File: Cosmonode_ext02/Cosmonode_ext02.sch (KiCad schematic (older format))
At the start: 19 parts, among them J1 CONN_01X04, J2 CONN_01X04, J3 CONN_01X08, J4 CONN_01X08, J5 GS3, J6 GS3, Q1 BSS138, Q2 BSS138, SW1 SW_Push, SW2 SW_Push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

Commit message: big push!
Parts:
- added J7: Aloes_Logo, Aloes:Aloes_mini, symbol CONN_01X01
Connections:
- net +5V: now also J1.1 (P1), J2.1 (P1); no longer J1.4 (P4), J2.4 (P4)
- net D3_5V: now also J1.2 (P2); no longer J1.3 (P3)
- net D4_5V: now also J2.2 (P2); no longer J2.3 (P3)
- net A6: now reaches J3.8 (P8)
- net A7: now reaches J4.8 (P8)
- net at C1.2, SW1.1: now also J1.4 (P4); no longer J1.1 (P1)
- net at C1.1, C2.2, C3.2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: now also J1.3 (P3), J2.3 (P3); no longer J1.2 (P2), J2.2 (P2)
- net at C5.2, SW2.1: now also J2.4 (P4); no longer J2.1 (P1)
- no-connect marks 6 -> 9
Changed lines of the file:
@@
 LIBS:valves
 LIBS:BSS138
-LIBS:XC6206P302MR_SOT23_
-LIBS:Cosmonode_ext02_v0.3-cache
+LIBS:Cosmonode_ext02-cache
 EELAYER 25 0
 EELAYER END
@@
 F 3 "" H 4200 2700 50  0001 C CNN
 	1    4200 2700
-	-1   0    0    1
+	-1   0    0    -1
 $EndComp
 $Comp
@@
 F 3 "" H 7250 2700 50  0001 C CNN
 	1    7250 2700
-	-1   0    0    1
+	-1   0    0    -1
 $EndComp
 $Comp
@@
 Text Notes 4250 2450 2    60   ~ 0
 SENSOR
+Text Label 7250 5400 2    60   ~ 0
+A6
+Text Label 8200 5400 2    60   ~ 0
+A7
+NoConn ~ 8200 5400
+NoConn ~ 7250 5400
+$Comp
+L CONN_01X01 J7
+U 1 1 59D33BEF
+P 4750 6050
+F 0 "J7" H 4750 6150 50  0000 C CNN
+F 1 "Aloes_Logo" V 4850 6050 50  0000 C CNN
+F 2 "Aloes:Aloes_mini" H 4750 6050 50  0001 C CNN
+F 3 "" H 4750 6050 50  0001 C CNN
+	1    4750 6050
+	1    0    0    -1
+$EndComp
+NoConn ~ 4550 6050
 $EndSCHEMATC

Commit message: big push2
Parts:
- added J8: OSHW_Logo, Symbols:OSHW-Logo_5.7x6mm_SilkScreen, symbol CONN_01X01
- J3, J4: footprint Pin_Headers:Pin_Header_Straight_1x08_Pitch2.54mm -> Socket_Strips:Socket_Strip_Straight_1x08_Pitch2.54mm
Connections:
- no-connect marks 9 -> 10
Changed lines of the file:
@@
 F 0 "J3" H 7450 5450 50  0000 C CNN
 F 1 "CONN_01X08" V 7550 5050 50  0000 C CNN
-F 2 "Pin_Headers:Pin_Header_Straight_1x08_Pitch2.54mm" H 7450 5050 50  0001 C CNN
+F 2 "Socket_Strips:Socket_Strip_Straight_1x08_Pitch2.54mm" H 7450 5050 50  0001 C CNN
 F 3 "" H 7450 5050 50  0001 C CNN
 	1    7450 5050
@@
 F 0 "J4" H 8400 5450 50  0000 C CNN
 F 1 "CONN_01X08" V 8500 5050 50  0000 C CNN
-F 2 "Pin_Headers:Pin_Header_Straight_1x08_Pitch2.54mm" H 8400 5050 50  0001 C CNN
+F 2 "Socket_Strips:Socket_Strip_Straight_1x08_Pitch2.54mm" H 8400 5050 50  0001 C CNN
 F 3 "" H 8400 5050 50  0001 C CNN
 	1    8400 5050
@@
 $EndComp
 NoConn ~ 4550 6050
+$Comp
+L CONN_01X01 J8
+U 1 1 59D41B96
+P 5250 6050
+F 0 "J8" H 5250 6150 50  0000 C CNN
+F 1 "OSHW_Logo" V 5350 6050 50  0000 C CNN
+F 2 "Symbols:OSHW-Logo_5.7x6mm_SilkScreen" H 5250 6050 50  0001 C CNN
+F 3 "" H 5250 6050 50  0001 C CNN
+	1    5250 6050
+	1    0    0    -1
+$EndComp
+NoConn ~ 5050 6050
 $EndSCHEMATC

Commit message: update to V0.7 (WIP)
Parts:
- J3, J4: value CONN_01X08 -> CONN_01X12; footprint Socket_Strips:Socket_Strip_Straight_1x08_Pitch2.54mm -> Socket_Strips:Socket_Strip_Straight_1x12_Pitch2.54mm; symbol CONN_01X08 -> CONN_01X12
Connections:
- net +3V3: no longer J4.3 (P3)
- net A0: now also J3.1 (P1), Q1.2 (S); no longer J3.6 (P6)
- net A1: now also J3.2 (P2), Q2.2 (S); no longer J3.7 (P7)
- net A4: now also J3.4 (P4); no longer J4.6 (P6)
- net A5: now also J3.5 (P5); no longer J4.7 (P7)
- net A6: now also J3.6 (P6); no longer J3.8 (P8)
- net A7: now also J3.7 (P7); no longer J4.8 (P8)
- net D3: now also J3.11 (P11); no longer J3.1 (P1), Q1.2 (S)
- net D4: now also J3.12 (P12); no longer J3.2 (P2), Q2.2 (S)
- net D5: now also J4.4 (P4); no longer J3.3 (P3), J5.1 (G1)
- net D6: now also J4.5 (P5); no longer J3.4 (P4)
- net D7: now also J4.6 (P6), J5.1 (G1); no longer J3.5 (P5)
- net GND: now also J4.3 (P3); no longer J4.4 (P4), J4.5 (P5)
- net BAT+ renamed +BATT
- net D3_5V renamed A0_5V
- net D4_5V renamed A1_5V
- new net A3: J3.3 (P3)
- new net D2: J3.10 (P10)
- new net D8: J4.7 (P7)
- new net D9: J4.8 (P8)
- new net MISO: J4.11 (P11)
- new net MOSI: J4.10 (P10)
- new net RST: J4.9 (P9)
- new net RX: J3.8 (P8)
- new net SCK: J4.12 (P12)
- new net TX: J3.9 (P9)
- no-connect marks 10 -> 19
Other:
- note added: "A0 5V output"
- note added: "D7 as +5V"
- note removed: "D3 5V input"
- note removed: "D5 as +5V"
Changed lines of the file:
@@
 LIBS:valves
 LIBS:BSS138
+LIBS:XC6206P302MR_SOT23_
 LIBS:Cosmonode_ext02-cache
 EELAYER 25 0
@@
 $EndDescr
 $Comp
-L CONN_01X08 J3
+L CONN_01X12 J3
 U 1 1 598047BC
 P 7450 5050
 F 0 "J3" H 7450 5450 50  0000 C CNN
-F 1 "CONN_01X08" V 7550 5050 50  0000 C CNN
-F 2 "Socket_Strips:Socket_Strip_Straight_1x08_Pitch2.54mm" H 7450 5050 50  0001 C CNN
+F 1 "CONN_01X12" V 7550 5050 50  0000 C CNN
+F 2 "Socket_Strips:Socket_Strip_Straight_1x12_Pitch2.54mm" H 7450 5050 50  0001 C CNN
 F 3 "" H 7450 5050 50  0001 C CNN
 	1    7450 5050
@@
 $EndComp
 $Comp
-L CONN_01X08 J4
-U 1 1 598047EF
-P 8400 5050
-F 0 "J4" H 8400 5450 50  0000 C CNN
-F 1 "CONN_01X08" V 8500 5050 50  0000 C CNN
-F 2 "Socket_Strips:Socket_Strip_Straight_1x08_Pitch2.54mm" H 8400 5050 50  0001 C CNN
-F 3 "" H 8400 5050 50  0001 C CNN
-	1    8400 5050
-	1    0    0    -1
-$EndComp
-Text Label 7250 4700 2    60   ~ 0
-D3
-Text Label 7250 4800 2    60   ~ 0
-D4
-Text Label 7250 4900 2    60   ~ 0
-D5
-Text Label 7250 5000 2    60   ~ 0
-D6
-Text Label 7250 5100 2    60   ~ 0
-D7
-Text Label 7250 5200 2    60   ~ 0
-A0
-Text Label 7250 5300 2    60   ~ 0
-A1
-Text Label 8200 4700 2    60   ~ 0
-BAT+
-$Comp
 L +3.3V #PWR01
 U 1 1 59804C25
-P 7850 4800
-F 0 "#PWR01" H 7850 4650 50  0001 C CNN
-F 1 "+3.3V" H 7850 4940 50  0000 C CNN
-F 2 "" H 7850 4800 50  0001 C CNN
-F 3 "" H 7850 4800 50  0001 C CNN
-	1    7850 4800
+P 7850 4550
+F 0 "#PWR01" H 7850 4400 50  0001 C CNN
+F 1 "+3.3V" H 7850 4690 50  0000 C CNN
+F 2 "" H 7850 4550 50  0001 C CNN
+F 3 "" H 7850 4550 50  0001 C CNN
+	1    7850 4550
 	1    0    0    -1
 $EndComp
@@
 L GND #PWR02
 U 1 1 59804C43
-P 7850 5100
-F 0 "#PWR02" H 7850 4850 50  0001 C CNN
-F 1 "GND" H 7850 4950 50  0000 C CNN
-F 2 "" H 7850 5100 50  0001 C CNN
-F 3 "" H 7850 5100 50  0001 C CNN
-	1    7850 5100
-	1    0    0    -1
-$EndComp
-Text Label 8200 5200 2    60   ~ 0
-A4
-Text Label 8200 5300 2    60   ~ 0
-A5
-Text Label 4050 3550 1    60   ~ 0
-D5
-Text Label 6500 3200 2    60   ~ 0
-D6
+P 7850 4700
+F 0 "#PWR02" H 7850 4450 50  0001 C CNN
+F 1 "GND" H 7850 4550 50  0000 C CNN
+F 2 "" H 7850 4700 50  0001 C CNN
+F 3 "" H 7850 4700 50  0001 C CNN
+	1    7850 4700
+	1    0    0    -1
+$EndComp
 Text Notes 4350 3400 2    60   ~ 0
-D5 as +5V
+D7 as +5V
 Text Notes 6850 3050 2    60   ~ 0
 D6 as GND
@@
 	-1   0    0    1
 $EndComp
-NoConn ~ 8200 4700
-NoConn ~ 7250 5300
-NoConn ~ 7250 5200
 $Comp
 L GND #PWR07
@@
 $EndComp
 Wire Wire Line
-	7850 5000 8200 5000
-Wire Wire Line
-	7850 5000 7850 5100
-Wire Wire Line
-	8200 5100 8150 5100
-Wire Wire Line
-	8150 5100 8150 5000
-Connection ~ 8150 5000
-Wire Wire Line
-	7850 4900 8200 4900
-Wire Wire Line
-	7850 4900 7850 4800
-Wire Wire Line
-	8200 4800 8150 4800
-Wire Wire Line
-	8150 4800 8150 4900
-Connection ~ 8150 4900
-Wire Wire Line
 	4400 2850 4900 2850
 Wire Wire Line
@@
 Connection ~ 5300 2750
 Connection ~ 5650 2750
-Text Label 6000 2400 2    60   ~ 0
-D3_5V
 Connection ~ 6000 2500
 Wire Wire Line
@@
 Connection ~ 8350 2750
 Connection ~ 8700 2750
-Text Label 9050 2400 2    60   ~ 0
-D4_5V
 Connection ~ 9050 2500
 Wire Wire Line
@@
 Wire Wire Line
 	9050 2750 9050 3600
-Text Notes 6300 2300 2    60   ~ 0
-D3 5V input
+Text Notes 6000 2150 2    60   ~ 0
+A0 5V output
 $Comp
 L PMIC-LDO-XC6206P302MR(SOT23) U1
@@
 	0    1    1    0
 $EndComp
-Text Label 4750 4950 0    60   ~ 0
-D4_5V
-Text Label 5850 4950 0    60   ~ 0
-D3_5V
-Text Label 5450 4950 2    60   ~ 0
-D3
-Text Label 4350 4950 2    60   ~ 0
-D4
 $Comp
 L +3.3V #PWR010
@@
 	0    1    1    0
 $EndComp
-NoConn ~ 8200 5200
-NoConn ~ 8200 5300
-NoConn ~ 7250 5100
 $Comp
 L +3.3V #PWR013
@@
 	1    0    0    -1
 $EndComp
-Text Notes 8350 5550 2    60   ~ 0
+Text Notes 8200 5850 2    60   ~ 0
 CONNECTORS TO NODE
 Text Notes 5500 5400 2    60   ~ 0
@@
 Text Notes 4250 2450 2    60   ~ 0
 SENSOR
-Text Label 7250 5400 2    60   ~ 0
-A6
-Text Label 8200 5400 2    60   ~ 0
-A7
-NoConn ~ 8200 5400
-NoConn ~ 7250 5400
 $Comp
 L CONN_01X01 J7
@@
 $EndComp
 NoConn ~ 5050 6050
+$Comp
+L +BATT #PWR014
+U 1 1 5A141DA3
+P 8100 4450
+F 0 "#PWR014" H 8100 4300 50  0001 C CNN
+F 1 "+BATT" H 8100 4590 50  0000 C CNN
+F 2 "" H 8100 4450 50  0001 C CNN
+F 3 "" H 8100 4450 50  0001 C CNN
+	1    8100 4450
+	1    0    0    -1
+$EndComp
+Wire Wire Line
+	8200 4500 8100 4500
+Wire Wire Line
+	8100 4500 8100 4450
+Wire Wire Line
+	7850 4700 8200 4700
+Wire Wire Line
+	8200 4600 7850 4600
+Wire Wire Line
+	7850 4600 7850 4550
+Text GLabel 8200 4800 0    51   BiDi ~ 0
+D5
+Text GLabel 8200 4900 0    51   BiDi ~ 0
+D6
+Text GLabel 8200 5000 0    51   BiDi ~ 0
+D7
+$Comp
+L CONN_01X12 J4
+U 1 1 598047EF
+P 8400 5050
+F 0 "J4" H 8400 5450 50  0000 C CNN
+F 1 "CONN_01X12" V 8500 5050 50  0000 C CNN
+F 2 "Socket_Strips:Socket_Strip_Straight_1x12_Pitch2.54mm" H 8400 5050 50  0001 C CNN
+F 3 "" H 8400 5050 50  0001 C CNN
+	1    8400 5050
+	1    0    0    -1
+$EndComp
+Text GLabel 8200 5100 0    51   BiDi ~ 0
+D8
+Text GLabel 8200 5200 0    51   BiDi ~ 0
+D9
+Text GLabel 8200 5300 0    51   BiDi ~ 0
+RST
+Text GLabel 8200 5400 0    51   BiDi ~ 0
+MOSI
+Text GLabel 8200 5500 0    51   BiDi ~ 0
+MISO
+Text GLabel 8200 5600 0    51   BiDi ~ 0
+SCK
+Text GLabel 7250 4500 0    51   BiDi ~ 0
+A0
+Text GLabel 7250 4600 0    51   BiDi ~ 0
+A1
+Text GLabel 7250 4700 0    51   BiDi ~ 0
+A3
+Text GLabel 7250 4800 0    51   BiDi ~ 0
+A4
+Text GLabel 7250 4900 0    51   BiDi ~ 0
+A5
+Text GLabel 7250 5000 0    51   BiDi ~ 0
+A6
+Text GLabel 7250 5100 0    51   BiDi ~ 0
+A7
+Text GLabel 7250 5200 0    51   BiDi ~ 0
+RX
+Text GLabel 7250 5300 0    51   BiDi ~ 0
+TX
+Text GLabel 7250 5400 0    51   BiDi ~ 0
+D2
+Text GLabel 7250 5500 0    51   BiDi ~ 0
+D3
+Text GLabel 7250 5600 0    51   BiDi ~ 0
+D4
+Text GLabel 4050 3550 0    51   BiDi ~ 0
+D7
+Text GLabel 6500 3200 0    51   BiDi ~ 0
+D6
+Text GLabel 5450 4950 0    51   BiDi ~ 0
+A0
+Text GLabel 4350 4950 0    51   BiDi ~ 0
+A1
+Text GLabel 4750 4950 2    51   BiDi ~ 0
+A1_5V
+Text GLabel 5850 4950 2    51   BiDi ~ 0
+A0_5V
+Text GLabel 6000 2400 1    51   BiDi ~ 0
+A0_5V
+Text GLabel 9050 2400 1    51   BiDi ~ 0
+A1_5V
+NoConn ~ 8200 5100
+NoConn ~ 8200 5200
+NoConn ~ 8200 5300
+NoConn ~ 8200 5400
+NoConn ~ 8200 5500
+NoConn ~ 8200 5600
+NoConn ~ 7250 5400
+NoConn ~ 7250 5300
+NoConn ~ 7250 5200
+NoConn ~ 7250 5100
+NoConn ~ 7250 5000
+NoConn ~ 7250 4700
+NoConn ~ 7250 4800
+NoConn ~ 7250 4900
+NoConn ~ 7250 5500
+NoConn ~ 7250 5600
+NoConn ~ 8200 4800
+$Comp
+L PWR_FLAG #FLG015
+U 1 1 5A1ED707
+P 9850 5100
+F 0 "#FLG015" H 9850 5175 50  0001 C CNN
+F 1 "PWR_FLAG" H 9850 5250 50  0000 C CNN
+F 2 "" H 9850 5100 50  0001 C CNN
+F 3 "" H 9850 5100 50  0001 C CNN
+	1    9850 5100
+	-1   0    0    1
+$EndComp
+$Comp
+L +BATT #PWR016
+U 1 1 5A1ED724
+P 9850 5100
+F 0 "#PWR016" H 9850 4950 50  0001 C CNN
+F 1 "+BATT" H 9850 5240 50  0000 C CNN
+F 2 "" H 9850 5100 50  0001 C CNN
+F 3 "" H 9850 5100 50  0001 C CNN
+	1    9850 5100
+	1    0    0    -1
+$EndComp
 $EndSCHEMATC

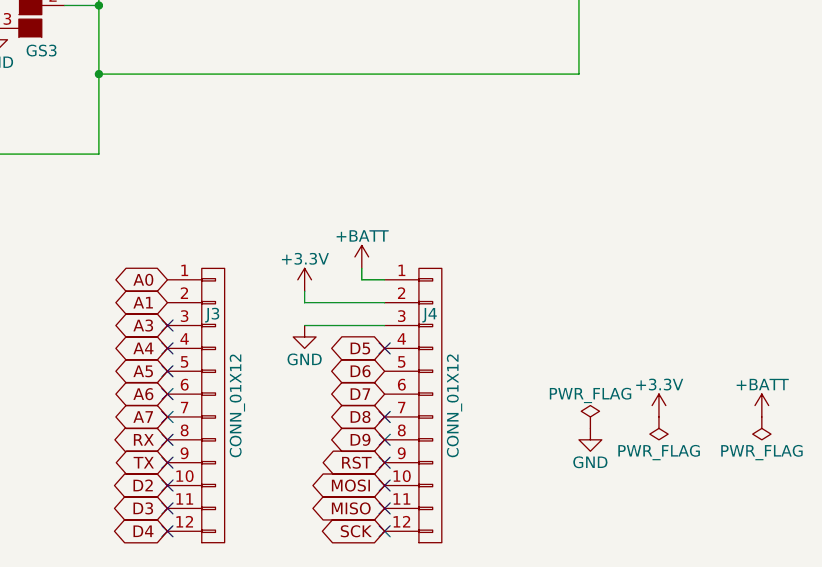
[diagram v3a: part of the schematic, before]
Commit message: near v0.7 ( mother and ext02 ), add mini extension
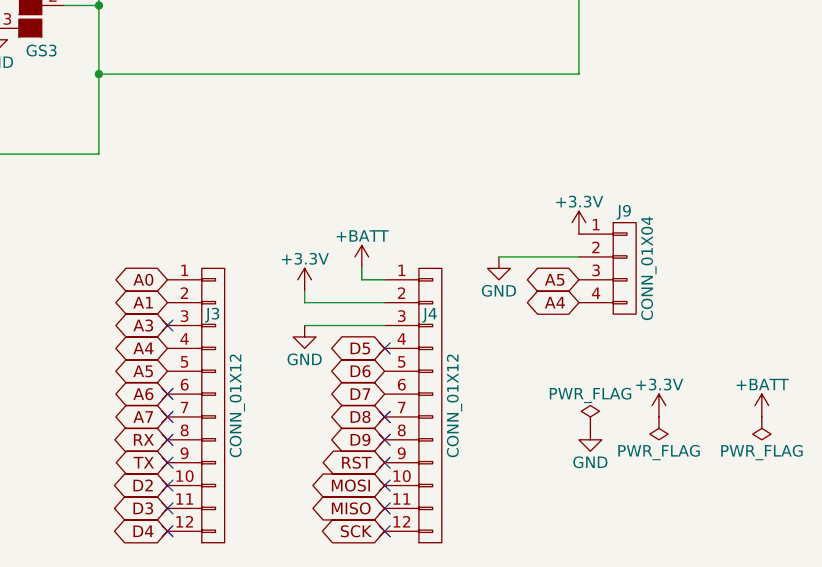
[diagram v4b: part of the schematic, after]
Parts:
- added J9: CONN_01X04, Socket_Strips:Socket_Strip_Straight_1x04_Pitch2.54mm, symbol CONN_01X04
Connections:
- net +3V3: now also J9.1 (P1)
- net A4: now also J9.4 (P4)
- net A5: now also J9.3 (P3)
- net GND: now also J9.2 (P2)
- no-connect marks 19 -> 17
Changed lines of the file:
@@
 Text GLabel 7250 4700 0    51   BiDi ~ 0
 A3
-Text GLabel 7250 4800 0    51   BiDi ~ 0
-A4
 Text GLabel 7250 4900 0    51   BiDi ~ 0
 A5
@@
 NoConn ~ 7250 5100
 NoConn ~ 7250 5000
-NoConn ~ 7250 4700
-NoConn ~ 7250 4800
-NoConn ~ 7250 4900
 NoConn ~ 7250 5500
 NoConn ~ 7250 5600
@@
 	1    0    0    -1
 $EndComp
+$Comp
+L CONN_01X04 J9
+U 1 1 5A2E9D5D
+P 9250 4450
+F 0 "J9" H 9250 4700 50  0000 C CNN
+F 1 "CONN_01X04" V 9350 4450 50  0000 C CNN
+F 2 "Socket_Strips:Socket_Strip_Straight_1x04_Pitch2.54mm" H 9250 4450 50  0001 C CNN
+F 3 "" H 9250 4450 50  0001 C CNN
+	1    9250 4450
+	1    0    0    -1
+$EndComp
+Text GLabel 9050 4500 0    51   BiDi ~ 0
+A5
+Text GLabel 9050 4600 0    51   BiDi ~ 0
+A4
+$Comp
+L +3.3V #PWR017
+U 1 1 5A2E9E4E
+P 9050 4300
+F 0 "#PWR017" H 9050 4150 50  0001 C CNN
+F 1 "+3.3V" H 9050 4440 50  0000 C CNN
+F 2 "" H 9050 4300 50  0001 C CNN
+F 3 "" H 9050 4300 50  0001 C CNN
+	1    9050 4300
+	1    0    0    -1
+$EndComp
+$Comp
+L GND #PWR018
+U 1 1 5A2E9E9B
+P 8700 4400
+F 0 "#PWR018" H 8700 4150 50  0001 C CNN
+F 1 "GND" H 8700 4250 50  0000 C CNN
+F 2 "" H 8700 4400 50  0001 C CNN
+F 3 "" H 8700 4400 50  0001 C CNN
+	1    8700 4400
+	1    0    0    -1
+$EndComp
+Wire Wire Line
+	9050 4400 8700 4400
+NoConn ~ 7250 4700
+Text GLabel 7250 4800 0    51   BiDi ~ 0
+A4
 $EndSCHEMATC

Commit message: fix and update
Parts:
- added J10: CONN_01X06, Pin_Headers:Pin_Header_Straight_1x06_Pitch2.54mm, symbol CONN_01X06
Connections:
- net +3V3: now also J10.1 (P1)
- net D5: now also J10.6 (P6)
- net GND: now also J10.2 (P2)
- net MISO: now also J10.4 (P4)
- net MOSI: now also J10.3 (P3)
- net SCK: now also J10.5 (P5)
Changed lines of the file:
@@
 Text GLabel 7250 4800 0    51   BiDi ~ 0
 A4
+$Comp
+L CONN_01X06 J10
+U 1 1 5A34520B
+P 10150 4100
+F 0 "J10" H 10150 4350 50  0000 C CNN
+F 1 "CONN_01X06" V 10250 4100 50  0000 C CNN
+F 2 "Pin_Headers:Pin_Header_Straight_1x06_Pitch2.54mm" H 10150 4100 50  0001 C CNN
+F 3 "" H 10150 4100 50  0001 C CNN
+	1    10150 4100
+	1    0    0    -1
+$EndComp
+$Comp
+L +3.3V #PWR019
+U 1 1 5A345213
+P 9950 3850
+F 0 "#PWR019" H 9950 3700 50  0001 C CNN
+F 1 "+3.3V" H 9950 3990 50  0000 C CNN
+F 2 "" H 9950 3850 50  0001 C CNN
+F 3 "" H 9950 3850 50  0001 C CNN
+	1    9950 3850
+	1    0    0    -1
+$EndComp
+$Comp
+L GND #PWR020
+U 1 1 5A345219
+P 9600 3950
+F 0 "#PWR020" H 9600 3700 50  0001 C CNN
+F 1 "GND" H 9600 3800 50  0000 C CNN
+F 2 "" H 9600 3950 50  0001 C CNN
+F 3 "" H 9600 3950 50  0001 C CNN
+	1    9600 3950
+	1    0    0    -1
+$EndComp
+Wire Wire Line
+	9950 3950 9600 3950
+Text GLabel 9950 4350 0    51   BiDi ~ 0
+D5
+Text GLabel 9950 4050 0    51   BiDi ~ 0
+MOSI
+Text GLabel 9950 4150 0    51   BiDi ~ 0
+MISO
+Text GLabel 9950 4250 0    51   BiDi ~ 0
+SCK
 $EndSCHEMATC
